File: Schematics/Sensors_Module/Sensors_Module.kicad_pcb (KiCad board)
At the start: 2 copper layers, 69.5 x 60 mm, 98 parts, among them J1 Stack Male Edge Connector, J2 SWD_01x04_Pin, J3 USB_C_Female_USB2_Small, J6 CAM_PWR, J7 CAM_DAT, Q1 AO3400A, Q2 AO3401A, Q3 AO3400A, SW1 SW_STM_RESET, SW2 SW_STM_BOOT_MODE, U1 LM66100DCKR, U10 AMS1117-3.3, U11 CP2102N-Axx-xQFN28, U12 BM1422AGMV, U2 ACS70331EOLC, U3 STM32F103CBT6, U5 LM66100DCKR, U6 LM66100DCKR, U7 ISO1042BDWVR, U8 W25Q128JVS, U9 BME680, Y1 X322516MMB4SI

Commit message: Completed PCB layout
Wow that was disgusting
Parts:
- removed TP10: PA4, TestPoint:TestPoint_Pad_1.5x1.5mm
- removed TP11: PA5, TestPoint:TestPoint_Pad_1.5x1.5mm
- removed TP12: PA6, TestPoint:TestPoint_Pad_1.5x1.5mm
- removed TP13: PB6, TestPoint:TestPoint_Pad_1.5x1.5mm
- removed TP14: PB5, TestPoint:TestPoint_Pad_1.5x1.5mm
- removed TP15: PB4, TestPoint:TestPoint_Pad_1.5x1.5mm
- removed TP16: PB7, TestPoint:TestPoint_Pad_1.5x1.5mm
- removed TP17: PA0, TestPoint:TestPoint_Pad_1.5x1.5mm
- removed TP2: TP_VUSB, TestPoint:TestPoint_Pad_1.5x1.5mm
- removed TP3: TP_VSWD, TestPoint:TestPoint_Pad_1.5x1.5mm
- removed TP4: TP_MUX, TestPoint:TestPoint_Pad_1.5x1.5mm
- removed TP5: TP_ISENSE, TestPoint:TestPoint_Pad_1.5x1.5mm
- removed TP8: TP_SCL, TestPoint:TestPoint_Pad_1.5x1.5mm
- removed TP9: TP_SDA, TestPoint:TestPoint_Pad_1.5x1.5mm
- added C11: 10uF, Capacitor_SMD:C_0603_1608Metric, F.Cu at (104.0, 52.2)
- added C16: 10uF, Capacitor_SMD:C_0603_1608Metric, F.Cu at (104.0, 56.4)
- added C17: 0.1u, Capacitor_SMD:C_0603_1608Metric, F.Cu at (95.1, 73.0)
- added C18: 20pF, Capacitor_SMD:C_0402_1005Metric, F.Cu at (112.0, 78.4)
- added C20: 20pF, Capacitor_SMD:C_0402_1005Metric, F.Cu at (112.0, 80.5)
- added C21: 0.1u, Capacitor_SMD:C_0603_1608Metric, F.Cu at (98.9, 60.5)
- added C36: 1uF, Capacitor_SMD:C_0603_1608Metric, F.Cu at (107.4, 64.1)
- added C37: 2.2uF, Capacitor_SMD:C_0603_1608Metric, F.Cu at (114.4, 63.3)
- added C38: 100p, Capacitor_SMD:C_0402_1005Metric, F.Cu at (96.2, 68.4)
- added C39: 0.1u, Capacitor_SMD:C_0603_1608Metric, F.Cu at (107.8, 73.0)
- added C40: 10uF, Capacitor_SMD:C_0603_1608Metric, F.Cu at (109.5, 73.0)
- added C41: 10uF, Capacitor_SMD:C_0603_1608Metric, F.Cu at (95.1, 79.5)
- added C42: 0.1u, Capacitor_SMD:C_0603_1608Metric, F.Cu at (95.1, 76.3)
- added C43: 47uF, Capacitor_SMD:C_0805_2012Metric, F.Cu at (96.2, 70.3)
- added C44: 100p, Capacitor_SMD:C_0402_1005Metric, F.Cu at (96.1, 82.8)
- added C45: 0.1u, Capacitor_SMD:C_0603_1608Metric, F.Cu at (96.1, 84.2)
- added C46: 100p, Capacitor_SMD:C_0402_1005Metric, F.Cu at (100.1, 82.8)
- added C47: 0.1u, Capacitor_SMD:C_0603_1608Metric, F.Cu at (100.1, 84.2)
- added C48: 100p, Capacitor_SMD:C_0402_1005Metric, F.Cu at (104.1, 82.8)
- added C49: 100p, Capacitor_SMD:C_0402_1005Metric, F.Cu at (108.1, 82.8)
- added C50: 0.1u, Capacitor_SMD:C_0603_1608Metric, F.Cu at (104.1, 84.2)
- added C51: 0.1u, Capacitor_SMD:C_0603_1608Metric, F.Cu at (108.1, 84.2)
- added C52: 100p, Capacitor_SMD:C_0402_1005Metric, F.Cu at (136.8, 82.8)
- added C53: 100p, Capacitor_SMD:C_0402_1005Metric, F.Cu at (141.3, 82.8)
- added C54: 100p, Capacitor_SMD:C_0402_1005Metric, F.Cu at (143.7, 82.8)
- added C55: 100p, Capacitor_SMD:C_0402_1005Metric, F.Cu at (146.8, 82.8)
- added C56: 0.1u, Capacitor_SMD:C_0603_1608Metric, F.Cu at (136.2, 84.2)
- added C57: 0.1u, Capacitor_SMD:C_0603_1608Metric, F.Cu at (139.9, 84.2)
- added C58: 0.1u, Capacitor_SMD:C_0603_1608Metric, F.Cu at (143.7, 84.2)
- added C59: 0.1u, Capacitor_SMD:C_0603_1608Metric, F.Cu at (147.4, 84.2)
- added C60: 20pF, Capacitor_SMD:C_0402_1005Metric, F.Cu at (140.6, 68.0)
- added C61: 20pF, Capacitor_SMD:C_0402_1005Metric, F.Cu at (147.8, 72.4)
- added C62: 47uF, Capacitor_SMD:C_0805_2012Metric, F.Cu at (136.2, 70.3)
- added C63: 0.1u, Capacitor_SMD:C_0603_1608Metric, F.Cu at (136.0, 68.3)
- added C64: 100p, Capacitor_SMD:C_0402_1005Metric, F.Cu at (135.2, 72.3)
- added C65: 10uF, Capacitor_SMD:C_0603_1608Metric, F.Cu at (147.8, 74.5)
- added C66: 0.1u, Capacitor_SMD:C_0603_1608Metric, F.Cu at (147.8, 77.6)
- added C67: 10uF, Capacitor_SMD:C_0402_1005Metric, F.Cu at (135.1, 78.3)
- added C68: 100n, Capacitor_SMD:C_0402_1005Metric, F.Cu at (135.1, 80.6)
- added J10: In, TerminalBlock_TE-Connectivity:TerminalBlock_TE_282834-2_1x02_P2.54mm_Horizontal, F.Cu at (129.5, 101.0)
- added J11: In, TerminalBlock_TE-Connectivity:TerminalBlock_TE_282834-2_1x02_P2.54mm_Horizontal, F.Cu at (136.1, 101.0)
- added J12: In, TerminalBlock_TE-Connectivity:TerminalBlock_TE_282834-2_1x02_P2.54mm_Horizontal, F.Cu at (142.7, 101.0)
- added J13: In, TerminalBlock_TE-Connectivity:TerminalBlock_TE_282834-2_1x02_P2.54mm_Horizontal, B.Cu at (146.5, 96.5)
- added J14: In, TerminalBlock_TE-Connectivity:TerminalBlock_TE_282834-2_1x02_P2.54mm_Horizontal, B.Cu at (139.9, 96.5)
- added J15: In, TerminalBlock_TE-Connectivity:TerminalBlock_TE_282834-2_1x02_P2.54mm_Horizontal, B.Cu at (133.3, 96.5)
- added J4: In, TerminalBlock_TE-Connectivity:TerminalBlock_TE_282834-2_1x02_P2.54mm_Horizontal, F.Cu at (98.2, 101.0)
- added J5: In, TerminalBlock_TE-Connectivity:TerminalBlock_TE_282834-2_1x02_P2.54mm_Horizontal, F.Cu at (104.8, 101.0)
- added J8: In, TerminalBlock_TE-Connectivity:TerminalBlock_TE_282834-2_1x02_P2.54mm_Horizontal, B.Cu at (106.0, 96.5)
- added J9: In, TerminalBlock_TE-Connectivity:TerminalBlock_TE_282834-2_1x02_P2.54mm_Horizontal, B.Cu at (99.4, 96.5)
- added JP1: CH1_BR, Jumper:SolderJumper-3_P1.3mm_Open_RoundedPad1.0x1.5mm, B.Cu at (96.5, 90.4)
- added JP2: CH2_BR, Jumper:SolderJumper-3_P1.3mm_Open_RoundedPad1.0x1.5mm, B.Cu at (101.3, 90.4)
- added JP3: CH3_BR, Jumper:SolderJumper-3_P1.3mm_Open_RoundedPad1.0x1.5mm, B.Cu at (106.1, 90.4)
- added JP4: CH4_BR, Jumper:SolderJumper-3_P1.3mm_Open_RoundedPad1.0x1.5mm, B.Cu at (110.9, 90.4)
- added JP5: CH5_BR, Jumper:SolderJumper-3_P1.3mm_Open_RoundedPad1.0x1.5mm, B.Cu at (132.0, 90.4)
- added JP6: CH6_BR, Jumper:SolderJumper-3_P1.3mm_Open_RoundedPad1.0x1.5mm, B.Cu at (136.8, 90.4)
- added JP7: CH7_BR, Jumper:SolderJumper-3_P1.3mm_Open_RoundedPad1.0x1.5mm, B.Cu at (141.6, 90.4)
- added JP8: CH8_BR, Jumper:SolderJumper-3_P1.3mm_Open_RoundedPad1.0x1.5mm, B.Cu at (146.4, 90.4)
- added R10: 350R, Resistor_SMD:R_0805_2012Metric_Pad1.20x1.40mm_HandSolder, F.Cu at (101.9, 89.0)
- added R11: 350, Resistor_SMD:R_0805_2012Metric_Pad1.20x1.40mm_HandSolder, F.Cu at (101.9, 93.0)
- added R13: 350R, Resistor_SMD:R_0805_2012Metric_Pad1.20x1.40mm_HandSolder, F.Cu at (106.7, 91.0)
- added R14: 350R, Resistor_SMD:R_0805_2012Metric_Pad1.20x1.40mm_HandSolder, F.Cu at (106.7, 89.0)
- added R15: 350, Resistor_SMD:R_0805_2012Metric_Pad1.20x1.40mm_HandSolder, F.Cu at (106.7, 93.0)
- added R16: 350R, Resistor_SMD:R_0805_2012Metric_Pad1.20x1.40mm_HandSolder, F.Cu at (111.5, 91.0)
- added R29: 350R, Resistor_SMD:R_0805_2012Metric_Pad1.20x1.40mm_HandSolder, F.Cu at (137.4, 91.0)
- added R30: 350R, Resistor_SMD:R_0805_2012Metric_Pad1.20x1.40mm_HandSolder, F.Cu at (137.4, 89.0)
- added R31: 350, Resistor_SMD:R_0805_2012Metric_Pad1.20x1.40mm_HandSolder, F.Cu at (137.4, 93.0)
- added R32: 350R, Resistor_SMD:R_0805_2012Metric_Pad1.20x1.40mm_HandSolder, F.Cu at (142.2, 91.0)
- added R33: 350R, Resistor_SMD:R_0805_2012Metric_Pad1.20x1.40mm_HandSolder, F.Cu at (142.2, 89.0)
- added R34: 350, Resistor_SMD:R_0805_2012Metric_Pad1.20x1.40mm_HandSolder, F.Cu at (142.2, 93.0)
- added R35: 350R, Resistor_SMD:R_0805_2012Metric_Pad1.20x1.40mm_HandSolder, F.Cu at (147.0, 91.0)
- added R36: 350R, Resistor_SMD:R_0805_2012Metric_Pad1.20x1.40mm_HandSolder, F.Cu at (147.0, 89.0)
- added R37: 350, Resistor_SMD:R_0805_2012Metric_Pad1.20x1.40mm_HandSolder, F.Cu at (147.0, 93.0)
- added R38: 10k, Resistor_SMD:R_0603_1608Metric, F.Cu at (107.4, 60.8)
- added R39: 10k, Resistor_SMD:R_0603_1608Metric, F.Cu at (147.8, 80.7)
- added R40: 10k, Resistor_SMD:R_0603_1608Metric, F.Cu at (112.0, 73.8)
- added R41: 49.9R, Resistor_SMD:R_0402_1005Metric, F.Cu at (96.2, 66.5)
- added R42: 49.9R, Resistor_SMD:R_0402_1005Metric, F.Cu at (95.1, 66.5)
- added R43: 100R, Resistor_SMD:R_0402_1005Metric, F.Cu at (114.9, 72.3)
- added R44: 100R, Resistor_SMD:R_0402_1005Metric, F.Cu at (113.9, 75.7)
- added R45: 100R, Resistor_SMD:R_0402_1005Metric, F.Cu at (111.4, 72.3)
- added R46: 330R, Resistor_SMD:R_0402_1005Metric, F.Cu at (95.1, 86.1)
- added R47: 330R, Resistor_SMD:R_0402_1005Metric, F.Cu at (97.1, 86.1)
- added R48: 330R, Resistor_SMD:R_0402_1005Metric, F.Cu at (99.1, 86.1)
- added R49: 330R, Resistor_SMD:R_0402_1005Metric, F.Cu at (101.1, 86.1)
- added R50: 330R, Resistor_SMD:R_0402_1005Metric, F.Cu at (103.1, 86.1)
- added R51: 330R, Resistor_SMD:R_0402_1005Metric, F.Cu at (105.1, 86.1)
- added R52: 330R, Resistor_SMD:R_0402_1005Metric, F.Cu at (107.1, 86.1)
- added R53: 330R, Resistor_SMD:R_0402_1005Metric, F.Cu at (109.1, 86.1)
- added R54: 330R, Resistor_SMD:R_0402_1005Metric, F.Cu at (135.2, 86.1)
- added R55: 330R, Resistor_SMD:R_0402_1005Metric, F.Cu at (137.2, 86.1)
- added R56: 330R, Resistor_SMD:R_0402_1005Metric, F.Cu at (138.9, 86.1)
- added R57: 330R, Resistor_SMD:R_0402_1005Metric, F.Cu at (140.9, 86.1)
- added R58: 330R, Resistor_SMD:R_0402_1005Metric, F.Cu at (142.7, 86.1)
- added R59: 330R, Resistor_SMD:R_0402_1005Metric, F.Cu at (144.7, 86.1)
- added R6: 350R, Resistor_SMD:R_0805_2012Metric_Pad1.20x1.40mm_HandSolder, F.Cu at (101.9, 91.0)
- added R60: 330R, Resistor_SMD:R_0402_1005Metric, F.Cu at (146.4, 86.1)
- added R61: 330R, Resistor_SMD:R_0402_1005Metric, F.Cu at (148.4, 86.1)
- added R62: 49.9R, Resistor_SMD:R_0402_1005Metric, F.Cu at (135.2, 76.2)
- added R63: 49.9R, Resistor_SMD:R_0402_1005Metric, F.Cu at (135.0, 66.4)
- added R64: 510R, Resistor_SMD:R_0603_1608Metric, F.Cu at (111.4, 70.1)
- added R65: 100k, Resistor_SMD:R_0603_1608Metric, F.Cu at (113.8, 69.8)
- added R66: 100R, Resistor_SMD:R_0402_1005Metric, F.Cu at (139.5, 70.8)
- added R67: 100R, Resistor_SMD:R_0402_1005Metric, F.Cu at (138.4, 70.8)
- added R68: 100R, Resistor_SMD:R_0402_1005Metric, F.Cu at (141.1, 70.8)
- added R69: 10k, Resistor_SMD:R_0603_1608Metric, F.Cu at (111.3, 57.3)
- added R70: 100k, Resistor_SMD:R_0402_1005Metric, F.Cu at (98.3, 66.3)
- added R71: 100k, Resistor_SMD:R_0402_1005Metric, F.Cu at (112.7, 64.2)
- added TH1: 10k, Resistor_SMD:R_0603_1608Metric_Pad0.98x0.95mm_HandSolder, F.Cu at (107.9, 57.3)
- added U13: OPA2727AIDR, footprints:SOIC127P599X175-8N-OPA2727, F.Cu at (102.6, 62.7)
- added U14: MCP1501-25xCH, Package_TO_SOT_SMD:SOT-23-6_Handsoldering, F.Cu at (110.9, 61.1)
- added U4: ADS1256IDBR, footprints:SOP65P780X200-28N, F.Cu at (101.4, 76.3)
- added Y2: X50328MSB2GI, footprints:CRYSTAL-SMD_L5.0-W3.2, F.Cu at (109.3, 78.4)
- added Y3: X50328MSB2GI, footprints:CRYSTAL-SMD_L5.0-W3.2, F.Cu at (145.4, 69.6)
- BZ1: value PKM13EPYH4000 -> PS1240P02BT; moved to B.Cu
- C15, C2: moved to B.Cu
- C28: value 1uF -> 0.1u
- C31: value 10uF -> 47uF; footprint Capacitor_SMD:C_0603_1608Metric -> Capacitor_SMD:C_0805_2012Metric
- C32: value 100nF -> 100uF; footprint Capacitor_SMD:C_0603_1608Metric -> Capacitor_SMD:C_1206_3216Metric
- C33: value 100nF -> 0.1u
- C34: value 1uF -> 47uF; footprint Capacitor_SMD:C_0603_1608Metric -> Capacitor_SMD:C_0805_2012Metric
- C35: value 1uF -> 100uF; footprint Capacitor_SMD:C_0603_1608Metric -> Capacitor_SMD:C_1206_3216Metric
- C6: value 0.1uF -> 100nF
- J2: footprint SWD_Header:SWD_PinHeader_1x04_P2.54mm_Horizontal -> SWD_Header:SWD_PinHeader_1x04_P2.54mm_Horizontal_SMD; moved to B.Cu
- J6: value CAM_PWR -> In
- J7: value CAM_DAT -> In; footprint TerminalBlock_TE-Connectivity:TerminalBlock_TE_282834-3_1x03_P2.54mm_Horizontal -> TerminalBlock_TE-Connectivity:TerminalBlock_TE_282834-2_1x02_P2.54mm_Horizontal; moved to B.Cu
- Q3: value AO3400A -> AO3401A
- R1: value 10k -> 350R; footprint Resistor_SMD:R_0603_1608Metric -> Resistor_SMD:R_0805_2012Metric_Pad1.20x1.40mm_HandSolder
- R2: value 510R -> 350; footprint Resistor_SMD:R_0603_1608Metric -> Resistor_SMD:R_0805_2012Metric_Pad1.20x1.40mm_HandSolder
- R21: value 4.7k -> 350R; footprint Resistor_SMD:R_0603_1608Metric -> Resistor_SMD:R_0805_2012Metric_Pad1.20x1.40mm_HandSolder
- R22: value 4.7k -> 350; footprint Resistor_SMD:R_0603_1608Metric -> Resistor_SMD:R_0805_2012Metric_Pad1.20x1.40mm_HandSolder
- R26, R27: value 100k -> 350R; footprint Resistor_SMD:R_0603_1608Metric -> Resistor_SMD:R_0805_2012Metric_Pad1.20x1.40mm_HandSolder
- R28: value 510 -> 350; footprint Resistor_SMD:R_0603_1608Metric -> Resistor_SMD:R_0805_2012Metric_Pad1.20x1.40mm_HandSolder
- R4: value 1k -> 350R; footprint Resistor_SMD:R_0603_1608Metric -> Resistor_SMD:R_0805_2012Metric_Pad1.20x1.40mm_HandSolder
- TP1: value TP_VSTACK -> VSTAK
- TP18: value PA1 -> PB11
- TP6: value TP_GND -> GND
- TP7: value TP_3V3 -> 3v3
- U12: value BM1422AGMV -> ADS1256IDBR; footprint Package_LGA:Rohm_MLGA010V020A_LGA-10_2x2mm_P0.45mm_LayoutBorder_3x2y -> footprints:SOP65P780X200-28N
- U2: value ACS70331EOLC -> TPM8837C-SO1R; footprint footprints:SOIC127P600X175-8N -> footprints:SOP-8_TPK
- U9: value BME680 -> AMS1117-5.0; footprint Package_LGA:Bosch_LGA-8_3x3mm_P0.8mm_ClockwisePinNumbering -> Package_TO_SOT_SMD:SOT-223-3_TabPin2
- moved U12 40.0 mm to (141.2, 76.8), turned to 90 degrees
- moved R26 37.3 mm to (132.6, 91.0), turned to 180 degrees
- moved U9 34.7 mm to (98.7, 54.3), turned to 180 degrees
- moved R4 34.4 mm to (97.1, 89.0)
- moved Q3 33.5 mm to (110.2, 65.2), turned to -90 degrees
- moved R3 33.1 mm to (115.2, 89.5)
- moved Q2 33.0 mm to (99.8, 69.3), turned to -90 degrees
- moved R28 32.3 mm to (132.6, 93.0), turned to 0 degrees
- moved BZ1 31.5 mm to (132.4, 61.5), turned to -45 degrees
- moved TP6 30.5 mm to (112.0, 86.3), turned to 90 degrees
- moved R27 29.6 mm to (132.6, 89.0)
- moved TP7 29.6 mm to (112.0, 83.5), turned to 90 degrees
- moved D3 28.5 mm to (115.8, 92.1)
- moved C31 28.2 mm to (105.1, 69.0), turned to -90 degrees
- moved C33 27.2 mm to (96.3, 62.0), turned to 180 degrees
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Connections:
- C2 pad 1: V_MUX -> +3.3V
- C28 pad 1: +3.3V -> 2.5VA_2
- C31 pad 1: CAM_5V -> 2.5VA_2
- C32 pad 1: +3.3V -> 2.5VA_2
- C33 pad 1: +3.3V -> 2.5VA_1
- C34 pad 1: Net-(U12-VREG) -> 2.5VA_1
- C35 pad 1: +3.3V -> 2.5VA_1
- C6 pad 1: V_MUX -> +3.3V
- D1 pad 1: Net-(BZ1--) -> Net-(D1-K)
- D1 pad 2: +BATT -> +3.3V
- D2 pad 1: Net-(BZ1--) -> Net-(D1-K)
- D2 pad 2: +3.3V -> +BATT
- D5 pad 1: GND -> Net-(D5-K)
- D5 pad 2: Net-(D5-A) -> DB_LED
- J6 pad 1: GND -> CH4_P
- J6 pad 2: CAM_5V -> CH4_L
- J7 pad 1: CAM_TX -> 2.5VA_WS_1
- J7 pad 2: CAM_RX -> CH3_P
- Q1 pad 3: Net-(BZ1-+) -> Net-(Q1-D)
- Q2 pad 1: Net-(Q2-G) -> Net-(Q1-D)
- Q2 pad 2: +5V -> 2.5VA_1
- Q2 pad 3: CAM_5V -> 2.5VA_WS_1
- Q3 pad 1: Net-(Q3-G) -> Net-(Q1-D)
- Q3 pad 2: GND -> 2.5VA_2
- Q3 pad 3: Net-(Q2-G) -> 2.5VA_WS_2
- R1 pad 1: GND -> 2.5VA_WS_1
- R1 pad 2: BUZZER -> CH1_N
- R17 pad 1: Net-(D5-A) -> GND
- R17 pad 2: DB_LED -> Net-(D5-K)
- R2 pad 1: Net-(Q1-G) -> CH1_P
- R2 pad 2: BUZZER -> Net-(JP1-A)
- R21 pad 1: +3.3V -> CH4_N
- R21 pad 2: SCL -> GND
- R22 pad 1: SDA -> CH4_P
- R22 pad 2: +3.3V -> Net-(JP4-A)
- R25 pad 2: GND -> +3.3V
- R26 pad 1: +5V -> 2.5VA_WS_2
- R26 pad 2: Net-(Q2-G) -> CH5_N
- R27 pad 1: CAM_PWR -> CH5_N
- R28 pad 1: CAM_PWR -> CH5_P
- R28 pad 2: Net-(Q3-G) -> Net-(JP5-A)
- R4 pad 1: Net-(BZ1-+) -> CH1_N
- R4 pad 2: Net-(BZ1--) -> GND
- TP18 pad 1: Net-(U3-PA1) -> Net-(U3-PB11)
- U1 pad 3: V_MUX -> +3.3V
- U1 pad 6: V_MUX -> +3.3V
- U12 pad 1: +3.3V -> +5VA
- U12 pad 10: +3.3V -> /ADC4B
- U12 pad 3: Net-(U12-VREG) -> Net-(U12-VREFN)
- U12 pad 4: unconnected-(U12-TEST1-Pad4) -> Net-(U12-VREFP)
- U12 pad 5: SDA -> GND
- U12 pad 6: unconnected-(U12-TEST2-Pad6) -> /ADC0B
- U12 pad 7: SCL -> /ADC1B
- U12 pad 8: unconnected-(U12-DRDY-Pad8) -> /ADC2B
- U12 pad 9: GND -> /ADC3B
- U2 pad 1: V_MUX -> Net-(D1-K)
- U2 pad 2: V_MUX -> Net-(BZ1-+)
- U2 pad 3: +3.3V -> Net-(BZ1--)
- U2 pad 4: +3.3V -> GND
- U2 pad 5: GND -> BUZZER_B
- U2 pad 6: unconnected-(U2-NC-Pad6) -> BUZZER_A
- U2 pad 7: CURR_SENSE -> +3.3V
- U2 pad 8: V_MUX -> +3.3V
- U3 pad 10: Net-(U3-PA0) -> TEMP
- U3 pad 11: Net-(U3-PA1) -> WS_EN
- U3 pad 14: Net-(U3-PA4) -> ADS1_CS
- U3 pad 15: Net-(U3-PA5) -> ADS_SCLK
- U3 pad 16: Net-(U3-PA6) -> ADS_DOUT
- U3 pad 17: BUZZER -> ADS_DIN
- U3 pad 18: CAM_PWR -> unconnected-(U3-PB0-Pad18)
- U3 pad 19: CURR_SENSE -> BUZZER_B
- U3 pad 21: SCL -> ADS1_DRDY
- U3 pad 22: SDA -> Net-(U3-PB11)
- U3 pad 29: RESET_FL -> unconnected-(U3-PA8-Pad29)
- U3 pad 30: CAM_TX -> unconnected-(U3-PA9-Pad30)
- U3 pad 31: CAM_RX -> BUZZER_A
- U3 pad 32: CAM_PWM -> RESET_FL
- U3 pad 39: RGB_DATA -> ADS2_CS
- U3 pad 40: Net-(U3-PB4) -> ADS2_DRDY
- U3 pad 41: Net-(U3-PB5) -> ADS_SYNC
- U3 pad 42: Net-(U3-PB6) -> ADS_RESET
- U3 pad 43: Net-(U3-PB7) -> RGB_DATA
- U5 pad 3: V_MUX -> +3.3V
- U5 pad 6: V_MUX -> +3.3V
- U6 pad 3: V_MUX -> +3.3V
- U6 pad 6: V_MUX -> +3.3V
- U9 pad 2: +3.3V -> +5VA
- U9 pad 3: SDA -> +BATT
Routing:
- net 2.5VA_WS_2: track 0.00 -> 157.9 mm, vias 0 -> 3
- net 2.5VA_WS_1: track 0.00 -> 99.8 mm, vias 0 -> 3
- net +5VA: track 0.00 -> 97.8 mm, vias 0 -> 18
- net GND: track 146.6 -> 239.3 mm, vias 98 -> 97
- net +5V: track 114.1 -> 21.6 mm
- net V_MUX: track 87.1 -> 0.00 mm
- net ADS_RESET: track 0.00 -> 57.4 mm, vias 0 -> 3
- net ADS_DOUT: track 0.00 -> 53.7 mm, vias 0 -> 3
- net 2.5VA_2: track 0.00 -> 52.5 mm, vias 0 -> 2
- net ADS_SYNC: track 0.00 -> 49.5 mm, vias 0 -> 3
- net CURR_SENSE: track 40.3 -> 0.00 mm, vias 4 -> 0
- net Net-(D4-DOUT): track 6.67 -> 44.8 mm
- net ADS_SCLK: track 0.00 -> 33.3 mm, vias 0 -> 2
- net CAM_PWR: track 31.8 -> 0.00 mm, vias 4 -> 0
- net ADS_DIN: track 0.00 -> 31.7 mm, vias 0 -> 2
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- added copper zone on B.Cu, net +5VA
- added copper zone on F.Cu, net +5VA
- added copper zone on In1.Cu, net GND
- added copper zone on In2.Cu, net GND
- removed copper zone on B.Cu, net GND
- removed copper zone on F.Cu, net GND
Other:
- copper layers 2 -> 4
- board text added: "1DN"
- board text added: "1DN 1CT"
- board text added: "1UP 3DN"
- board text added: "2DN"
- board text added: "2DN 4UP"
- board text added: "2UP 2CT"
- board text added: "3CT 3UP"
- board text added: "3DN"
- board text added: "4CT 4DN"
- board text added: "4DN"
- board text added: "5DN"
- board text added: "5DN 5CT"
- board text added: "5UP 7DN"
- board text added: "6DN"
- board text added: "6DN 8UP"
- board text added: "6UP 6CT"
- board text added: "7CT 7UP"
- board text added: "7DN"
- board text added: "8CT 8DN"
- board text added: "8DN"
- board text added: "Int Ext"
- board text added: "PB-FREE"
- board text added: "PWR"
- board text added: "STAT"
- board text added: "locked"
- board text added: "now THIS is the most annoying layout we've ever had."
- board text removed: "-CAM+"
- board text removed: "."
- board text removed: "Cotija Rev 2.0 QRET Mar 2025 Ethan Toste Kennan Bays"
- board text removed: "PM TX RX"
- board text removed: "POWER"
- board text removed: "STATUS"

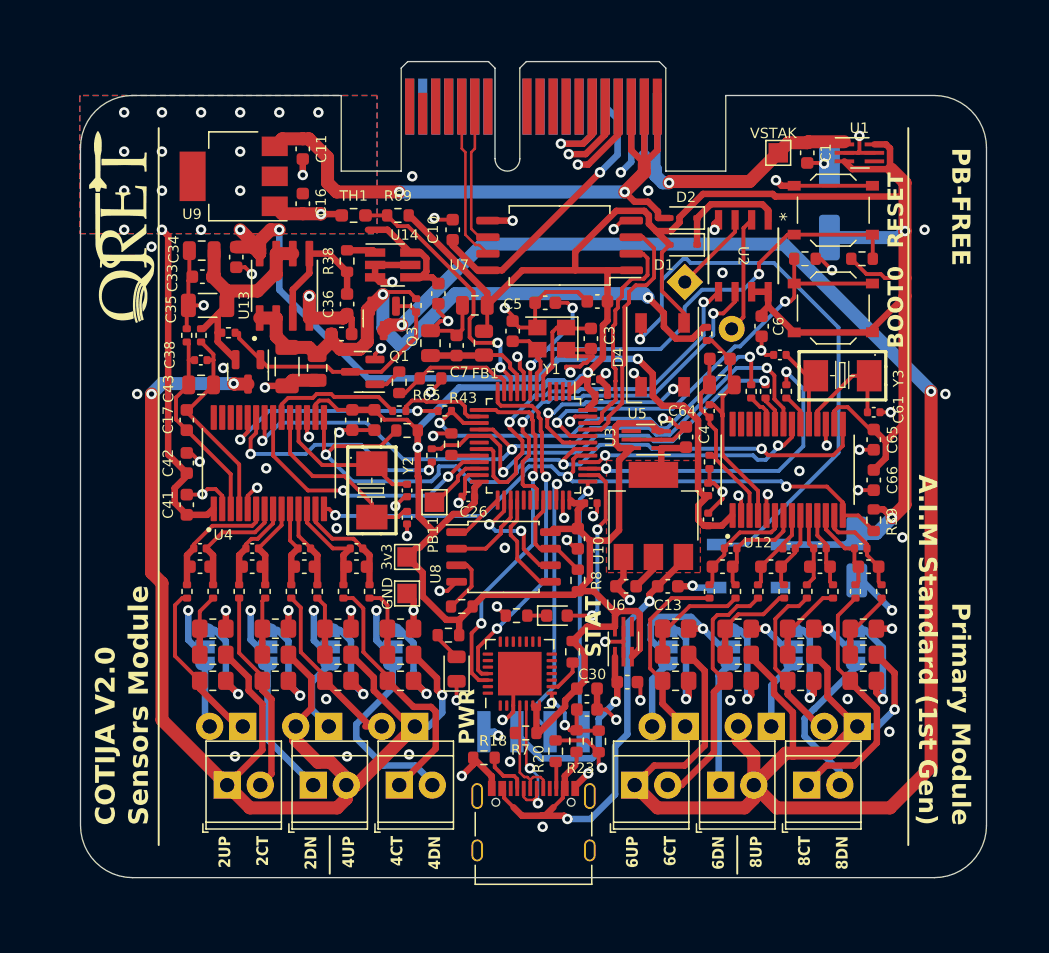
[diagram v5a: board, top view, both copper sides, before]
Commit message: Final silkscreen adjustment
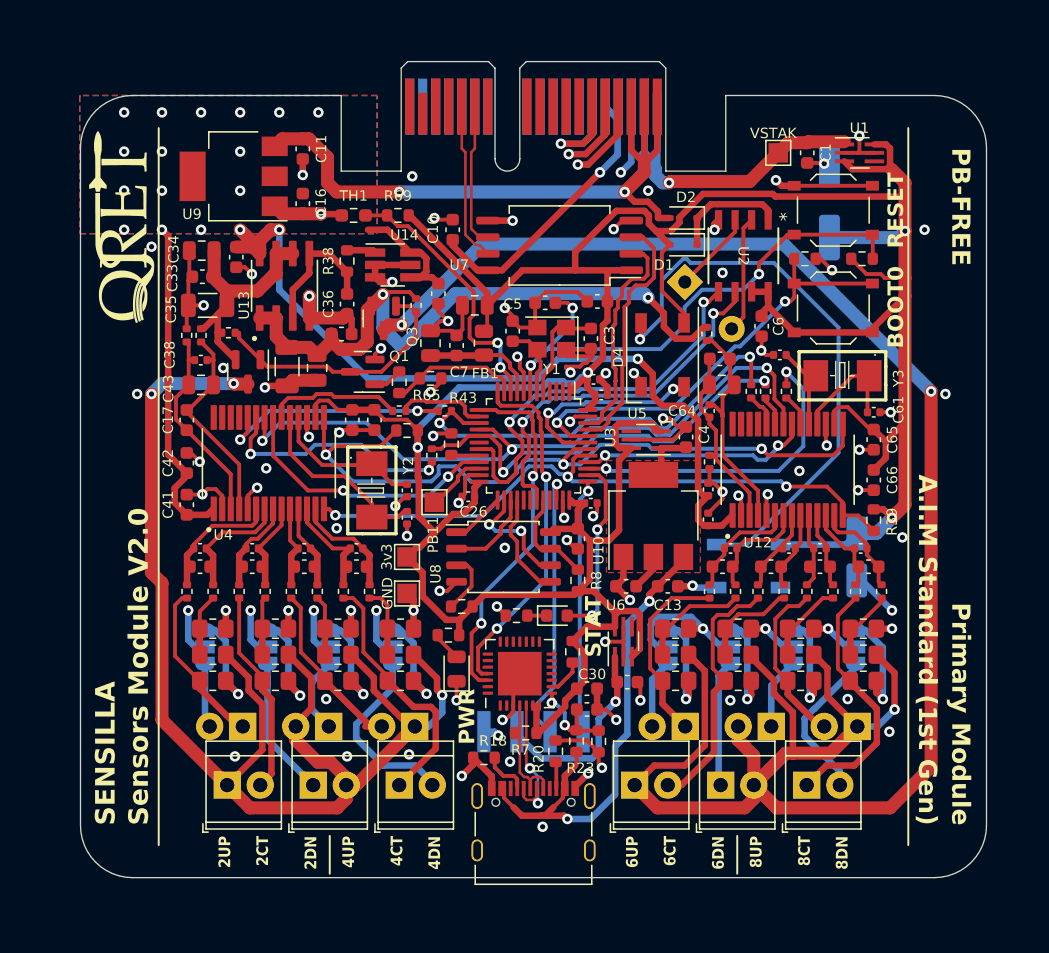
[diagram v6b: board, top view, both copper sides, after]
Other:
- board text added: "SENSILLA"
- board text added: "Sensors Module V2.0"
- board text removed: "COTIJA V2.0"
- board text removed: "Sensors Module"
